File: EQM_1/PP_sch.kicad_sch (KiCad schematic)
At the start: 4 parts, among them Q1 Q_NMOS_GDSD, Q2 Q_PMOS_GDSD

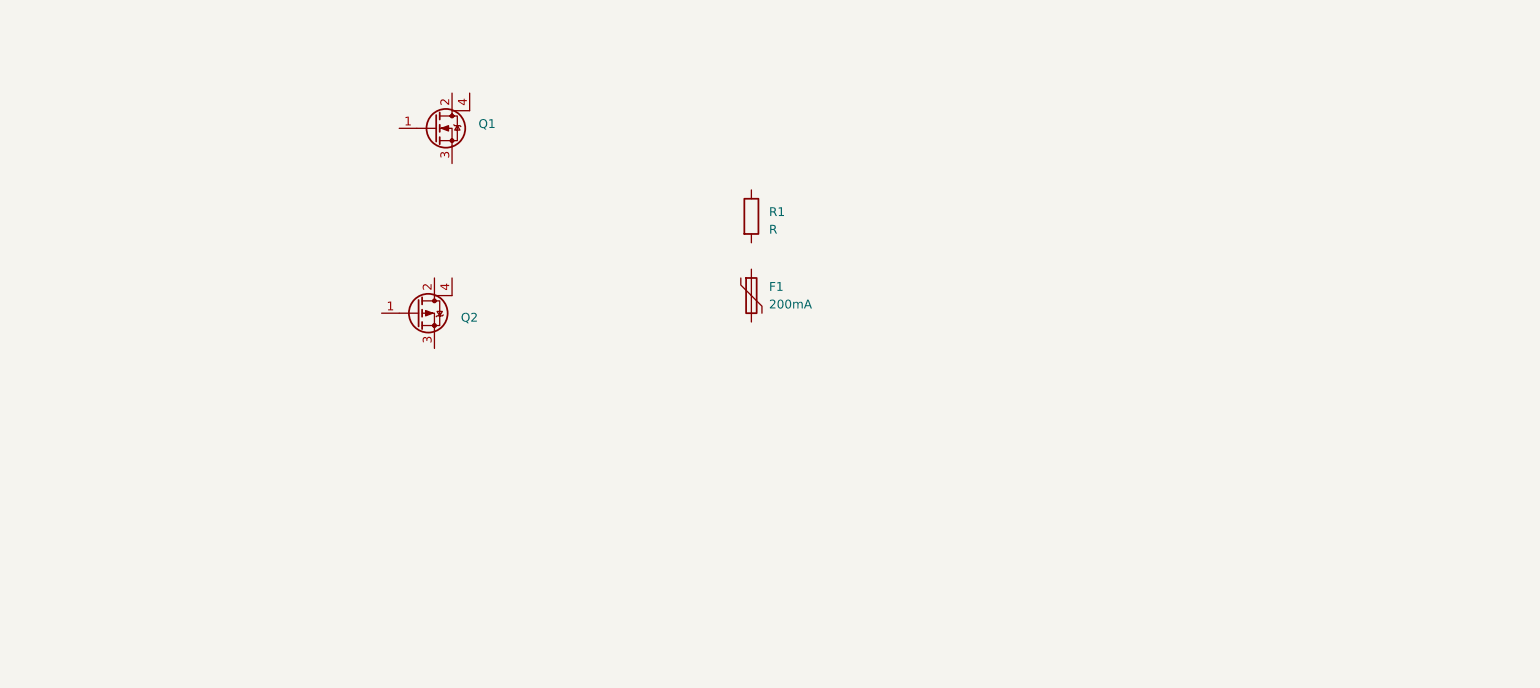
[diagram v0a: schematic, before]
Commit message: Temperatura
Se ha añadido el circuito del sensor de temperatura
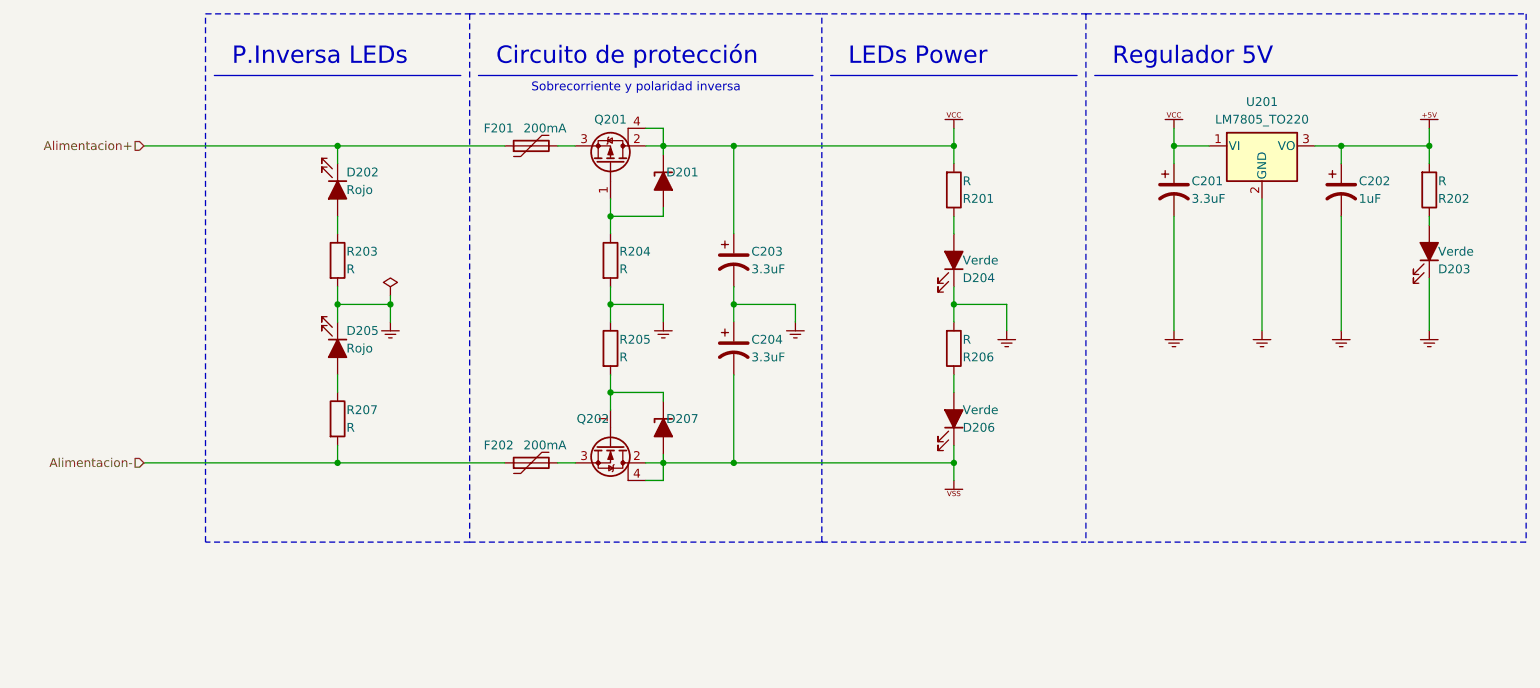
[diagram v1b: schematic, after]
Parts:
- removed Q1: Q_NMOS_GDSD, symbol Device:Q_NMOS_GDSD
- added C201, C203, C204: 3.3uF, Capacitor_SMD:C_0201_0603Metric, symbol Device:C_Polarized_US
- added C202: 1uF, Capacitor_SMD:C_0201_0603Metric, symbol Device:C_Polarized_US
- added D201, D207: D_Zener_Filled, symbol Device:D_Zener_Filled
- added D202, D203, D204, D205, D206: LED_Filled, symbol Device:LED_Filled
- added F202: 200mA, symbol Device:Polyfuse
- added Q202: Q_NMOS_GDSD, symbol Device:Q_NMOS_GDSD
- added R201, R202, R203, R205, R206, R207: R, symbol Device:R
- added U201: LM7805_TO220, Package_TO_SOT_THT:TO-220-3_Vertical, symbol Regulator_Linear:LM7805_TO220
- renumbered F1 to F201, Q2 to Q201, R1 to R204
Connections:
- net at Q201.1 (G): now also R204.1, D201.2 (A)
- net VCC: now reaches Q201.2 (D)
- net VCC: now also Q201.4 (D), C201.1, C203.1, D201.1 (K), R201.2, U201.1 (VI)
- net at Q201.3 (S): now also F201.2
- net Alimentacion+: now reaches F201.1
- net Alimentacion+: now also D202.1 (K)
- net GND: now reaches R204.2
- net GND: now also C201.2, C202.2, C203.2, C204.1, D203.1 (K), D204.1 (K), D205.1 (K), R203.2, R205.1, R206.2, U201.2 (GND)
- new net: F202.2, Q202.3 (S)
- new net: D207.1 (K), Q202.1 (G), R205.2
- new net: D203.2 (A), R202.1
- new net: D206.2 (A), R206.1
- new net: D204.2 (A), R201.1
- new net: D202.2 (A), R203.1
- new net: D205.2 (A), R207.1
- new net #VSS: C204.2, D206.1 (K), D207.2 (A), Q202.2 (D), Q202.4 (D)
- new net +5V: C202.1, R202.2, U201.3 (VO)
- new net Alimentacion-: F202.1, R207.2
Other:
- note added: "Circuito de protección"
- note added: "LEDs Power"
- note added: "P.Inversa LEDs"
- note added: "Regulador 5V"
- note added: "Sobrecorriente y polaridad inversa"
- moved on the sheet: F201, Q201, R204

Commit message: Esquema finalizado
El esquema está finalizado a falta de la asociación de footprints y la selección de valores para los pasivos
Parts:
- added J101: Screw_Terminal_01x03, symbol Connector:Screw_Terminal_01x03
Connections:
- net GND: now also J101.2 (Pin_2)
- net Alimentacion+: no longer names the net of D202.1 (K), F201.1
- net Alimentacion+: now also J101.1 (Pin_1)
- net Alimentacion-: no longer names the net of F202.1, R207.2
- net Alimentacion-: now also J101.3 (Pin_3)
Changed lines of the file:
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@@
     (rev "V0.1-Alpha")
     (company "JSM - ETSE-UV")
+    (comment 1 "Alimentación y protecciones")
   )
   (junction (at 227.33 57.15) (diameter 0) (color 0 0 0 0)
@@
     (stroke (width 0) (type default))
   )
-  (wire (pts (xy 41.91 57.15) (xy 69.85 57.15))
-    (stroke (width 0) (type default))
-  )
-  (wire (pts (xy 69.85 57.15) (xy 93.98 57.15))
+  (wire (pts (xy 39.37 57.15) (xy 69.85 57.15))
     (stroke (width 0) (type default))
   )
@@
     (stroke (width 0) (type default))
   )
+  (wire (pts (xy 44.45 59.69) (xy 39.37 59.69))
+    (stroke (width 0) (type default))
+  )
   (polyline (pts (xy 88.9 38.1) (xy 139.7 38.1))
     (stroke (width 0) (type dash))
@@
     (stroke (width 0) (type default))
   )
+  (wire (pts (xy 69.85 57.15) (xy 93.98 57.15))
+    (stroke (width 0) (type default))
+  )
   (wire (pts (xy 214.63 67.31) (xy 214.63 83.82))
     (stroke (width 0) (type default))
@@
     (stroke (width 0) (type default))
   )
+  (wire (pts (xy 41.91 62.23) (xy 41.91 102.87))
+    (stroke (width 0) (type default))
+  )
   (wire (pts (xy 109.22 64.77) (xy 109.22 67.31))
     (stroke (width 0) (type default))
@@
     (stroke (width 0) (type dash))
   )
+  (wire (pts (xy 39.37 62.23) (xy 41.91 62.23))
+    (stroke (width 0) (type default))
+  )
   (wire (pts (xy 158.75 100.33) (xy 158.75 102.87))
     (stroke (width 0) (type default))
@@
   )
   (wire (pts (xy 69.85 57.15) (xy 69.85 59.69))
+    (stroke (width 0) (type default))
+  )
+  (wire (pts (xy 44.45 62.23) (xy 44.45 59.69))
     (stroke (width 0) (type default))
   )
@@
     (effects (font (size 1.27 1.27)) (justify left bottom))
   )
-  (hierarchical_label "Alimentacion-" (shape input) (at 41.91 102.87 180) (fields_autoplaced)
-    (effects (font (size 1.27 1.27)) (justify right))
-  )
-  (hierarchical_label "Alimentacion+" (shape input) (at 41.91 57.15 180) (fields_autoplaced)
-    (effects (font (size 1.27 1.27)) (justify right))
-  )
   (symbol (lib_id "CPower:VCC") (at 190.5 53.34 0) (unit 1)
     (in_bom no) (on_board no) (dnp no) (fields_autoplaced)
@@
     )
   )
+  (symbol (lib_id "Connector:Screw_Terminal_01x03") (at 34.29 59.69 0) (mirror y) (unit 1)
+    (in_bom yes) (on_board yes) (dnp no)
+    (property "Reference" "J101" (at 35.56 54.61 0)
+      (effects (font (size 1.27 1.27)))
+    )
+    (property "Value" "Screw_Terminal_01x03" (at 31.7972 61.595 0)
+      (effects (font (size 1.27 1.27)) (justify left) hide)
+    )
+    (property "Footprint" "" (at 34.29 59.69 0)
+      (effects (font (size 1.27 1.27)) hide)
+    )
+    (property "Datasheet" "~" (at 34.29 59.69 0)
+      (effects (font (size 1.27 1.27)) hide)
+    )
+    (property "Use" "PWR in" (at 27.94 59.69 0)
+      (effects (font (size 1.27 1.27)))
+    )
+    (pin "1")
+    (pin "2")
+    (pin "3")
+    (instances
+      (project "EQM_1"
+        (path "/de1eb2e3-111e-4110-973a-00c5643131f3"
+          (reference "J101") (unit 1)
+        )
+        (path "/de1eb2e3-111e-4110-973a-00c5643131f3/e93d5772-2a4a-4e62-9fe9-f443f30f8fbe"
+          (reference "J201") (unit 1)
+        )
+      )
+    )
+  )
   (symbol (lib_id "Device:LED_Filled") (at 158.75 96.52 270) (mirror x) (unit 1)
     (in_bom yes) (on_board yes) (dnp no)
@@
   (symbol (lib_id "CPower:#GND") (at 190.5 83.82 0) (mirror y) (unit 1)
     (in_bom no) (on_board no) (dnp no) (fields_autoplaced)
-    (property "Reference" "#gnd0205" (at 190.5 83.82 0)
+    (property "Reference" "#gnd0206" (at 190.5 83.82 0)
       (effects (font (size 1.27 1.27)) hide)
     )
@@
       (project "EQM_1"
         (path "/de1eb2e3-111e-4110-973a-00c5643131f3/e93d5772-2a4a-4e62-9fe9-f443f30f8fbe"
-          (reference "#gnd0205") (unit 1)
+          (reference "#gnd0206") (unit 1)
         )
       )
@@
   (symbol (lib_id "CPower:#GND") (at 227.33 83.82 0) (mirror y) (unit 1)
     (in_bom no) (on_board no) (dnp no) (fields_autoplaced)
-    (property "Reference" "#gnd0208" (at 227.33 83.82 0)
+    (property "Reference" "#gnd0209" (at 227.33 83.82 0)
       (effects (font (size 1.27 1.27)) hide)
     )
@@
       (project "EQM_1"
         (path "/de1eb2e3-111e-4110-973a-00c5643131f3/e93d5772-2a4a-4e62-9fe9-f443f30f8fbe"
-          (reference "#gnd0208") (unit 1)
+          (reference "#gnd0209") (unit 1)
         )
       )
@@
   (symbol (lib_id "CPower:#GND") (at 166.37 83.82 0) (mirror y) (unit 1)
     (in_bom no) (on_board no) (dnp no) (fields_autoplaced)
-    (property "Reference" "#gnd0204" (at 166.37 83.82 0)
+    (property "Reference" "#gnd0205" (at 166.37 83.82 0)
       (effects (font (size 1.27 1.27)) hide)
     )
@@
       (project "EQM_1"
         (path "/de1eb2e3-111e-4110-973a-00c5643131f3/e93d5772-2a4a-4e62-9fe9-f443f30f8fbe"
-          (reference "#gnd0204") (unit 1)
+          (reference "#gnd0205") (unit 1)
         )
       )
@@
   (symbol (lib_id "CPower:#GND") (at 214.63 83.82 0) (mirror y) (unit 1)
     (in_bom no) (on_board no) (dnp no) (fields_autoplaced)
-    (property "Reference" "#gnd0207" (at 214.63 83.82 0)
+    (property "Reference" "#gnd0208" (at 214.63 83.82 0)
       (effects (font (size 1.27 1.27)) hide)
     )
@@
       (project "EQM_1"
         (path "/de1eb2e3-111e-4110-973a-00c5643131f3/e93d5772-2a4a-4e62-9fe9-f443f30f8fbe"
-          (reference "#gnd0207") (unit 1)
+          (reference "#gnd0208") (unit 1)
         )
       )
@@
   (symbol (lib_id "CPower:#GND") (at 203.2 83.82 0) (mirror y) (unit 1)
     (in_bom no) (on_board no) (dnp no) (fields_autoplaced)
-    (property "Reference" "#gnd0206" (at 203.2 83.82 0)
+    (property "Reference" "#gnd0207" (at 203.2 83.82 0)
       (effects (font (size 1.27 1.27)) hide)
     )
@@
       (project "EQM_1"
         (path "/de1eb2e3-111e-4110-973a-00c5643131f3/e93d5772-2a4a-4e62-9fe9-f443f30f8fbe"
-          (reference "#gnd0206") (unit 1)
+          (reference "#gnd0207") (unit 1)
         )
       )
@@
   (symbol (lib_id "CPower:#GND") (at 116.84 82.55 0) (unit 1)
     (in_bom no) (on_board no) (dnp no) (fields_autoplaced)
-    (property "Reference" "#gnd0202" (at 116.84 82.55 0)
+    (property "Reference" "#gnd0203" (at 116.84 82.55 0)
       (effects (font (size 1.27 1.27)) hide)
     )
@@
       (project "EQM_1"
         (path "/de1eb2e3-111e-4110-973a-00c5643131f3/e93d5772-2a4a-4e62-9fe9-f443f30f8fbe"
-          (reference "#gnd0202") (unit 1)
+          (reference "#gnd0203") (unit 1)
         )
       )
@@
   (symbol (lib_id "CPower:#GND") (at 77.47 82.55 0) (unit 1)
     (in_bom no) (on_board no) (dnp no) (fields_autoplaced)
-    (property "Reference" "#gnd0201" (at 77.47 82.55 0)
+    (property "Reference" "#gnd0202" (at 77.47 82.55 0)
       (effects (font (size 1.27 1.27)) hide)
     )
@@
       (project "EQM_1"
         (path "/de1eb2e3-111e-4110-973a-00c5643131f3/e93d5772-2a4a-4e62-9fe9-f443f30f8fbe"
-          (reference "#gnd0201") (unit 1)
+          (reference "#gnd0202") (unit 1)
         )
       )
@@
   (symbol (lib_id "CPower:#GND") (at 135.89 82.55 0) (unit 1)
     (in_bom no) (on_board no) (dnp no) (fields_autoplaced)
-    (property "Reference" "#gnd0203" (at 135.89 82.55 0)
+    (property "Reference" "#gnd0204" (at 135.89 82.55 0)
       (effects (font (size 1.27 1.27)) hide)
     )
@@
       (project "EQM_1"
         (path "/de1eb2e3-111e-4110-973a-00c5643131f3/e93d5772-2a4a-4e62-9fe9-f443f30f8fbe"
-          (reference "#gnd0203") (unit 1)
-        )
-      )
+          (reference "#gnd0204") (unit 1)
+        )
+      )
+    )
+  )
+  (symbol (lib_id "CPower:#GND") (at 44.45 62.23 0) (unit 1)
+    (in_bom no) (on_board no) (dnp no) (fields_autoplaced)
+    (property "Reference" "#gnd0101" (at 44.45 62.23 0)
+      (effects (font (size 1.27 1.27)) hide)
+    )
+    (property "Value" "#GND" (at 44.45 62.23 0)
+      (effects (font (size 1.27 1.27)) hide)
+    )
+    (property "Footprint" "" (at 44.45 62.23 0)
+      (effects (font (size 1.27 1.27)) hide)
+    )
+    (property "Datasheet" "" (at 44.45 62.23 0)
+      (effects (font (size 1.27 1.27)) hide)
+    )
+    (pin "1")
+    (instances
+      (project "EQM_1"
+        (path "/de1eb2e3-111e-4110-973a-00c5643131f3"
+          (reference "#gnd0101") (unit 1)
+        )
+        (path "/de1eb2e3-111e-4110-973a-00c5643131f3/e93d5772-2a4a-4e62-9fe9-f443f30f8fbe"
+          (reference "#gnd0201") (unit 1)
+        )
+      )

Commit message: PCB-1
Primer posicionamiento de los componentes en la pcb y ligeros cambios en el esquemático.
Posicionamiento MUY BASTO, simplemente para ver que los componentes caben en las dimensiones de la pcb elegida.
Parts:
- removed C201, C203, C204: 3.3uF, Capacitor_SMD:C_0201_0603Metric, symbol Device:C_Polarized_US
- removed C202: 1uF, Capacitor_SMD:C_0201_0603Metric, symbol Device:C_Polarized_US
- added C303 (x4): 3.3uF, Capacitor_SMD:C_0805_2012Metric_Pad1.18x1.45mm_HandSolder, symbol Device:C
- added D205, D206: 1n4007, Diode_SMD:D_0805_2012Metric_Pad1.15x1.40mm_HandSolder, symbol Device:D_Filled
- D201: value D_Zener_Filled -> 5.1V; footprint (none) -> Diode_SMD:D_0805_2012Metric_Pad1.15x1.40mm_HandSolder
- D202, D203, D204: footprint (none) -> Diode_SMD:D_0805_2012Metric_Pad1.15x1.40mm_HandSolder
- D207: renamed from D205; footprint (none) -> Diode_SMD:D_0805_2012Metric_Pad1.15x1.40mm_HandSolder
- D208: renamed from D206; footprint (none) -> Diode_SMD:D_0805_2012Metric_Pad1.15x1.40mm_HandSolder
- D209: renamed from D207; value D_Zener_Filled -> 5.1V; footprint (none) -> Diode_SMD:D_0805_2012Metric_Pad1.15x1.40mm_HandSolder
- F201, F202: footprint (none) -> Diode_SMD:D_1210_3225Metric_Pad1.42x2.65mm_HandSolder
- J101: footprint (none) -> TerminalBlock_Phoenix:TerminalBlock_Phoenix_MKDS-1,5-3-5.08_1x03_P5.08mm_Horizontal
- Q201, Q202: footprint (none) -> Package_TO_SOT_SMD:SOT-223
- R201, R203, R206, R207: value R -> 1K5; footprint (none) -> Resistor_SMD:R_0805_2012Metric_Pad1.20x1.40mm_HandSolder
- R202: value R -> 670R; footprint (none) -> Resistor_SMD:R_0805_2012Metric_Pad1.20x1.40mm_HandSolder
- R204, R205: value R -> 10K; footprint (none) -> Resistor_SMD:R_0805_2012Metric_Pad1.20x1.40mm_HandSolder
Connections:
- net +5V: now also C303.1
- net GND: now also D202.2 (A), D208.2 (A), C303.1, C303.2, C303.2, C303.2; no longer R203.2, R206.2
- net VCC: now also Q201.3 (S), C303.1, C303.1; no longer Q201.2 (D), Q201.4 (D)
- net at F202.2: now also Q202.2 (D), Q202.4 (D); no longer Q202.3 (S)
- net at F201.1, J101.1 (Pin_1): now also R203.1; no longer D202.1 (K)
- net VSS: now reaches R206.1
- net VSS: now also D209.2 (A), Q202.3 (S), C303.2; no longer D208.2 (A)
- net at F201.2: now also Q201.2 (D), Q201.4 (D); no longer Q201.3 (S)
- net at D207.2 (A): now also D206.1 (K); no longer R207.1
- removed net #VSS: D208.1 (K), D209.2 (A), Q202.2 (D), Q202.4 (D)
- new net: D205.1 (K), R203.2
- new net: D202.1 (K), D205.2 (A)
- new net: D208.1 (K), R206.2
- new net: D206.2 (A), R207.1
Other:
- moved on the sheet: D202, D207, D208, D209, F202, Q201, Q202, R203, R205, R206, R207
